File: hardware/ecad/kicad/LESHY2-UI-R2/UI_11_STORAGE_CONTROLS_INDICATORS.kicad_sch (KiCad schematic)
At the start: 107 parts, among them J4 Hirose DF40C(2.0)-40DS-0.4V(5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, J5 Hirose DM3AT-SF-PEJM5, Q1 Diodes Incorporated DMN2056U-7, SW10 OMRON B3S-1100P, SW11 OMRON B3S-1100P, SW12 OMRON B3S-1100P, SW13 OMRON B3S-1100P, SW14 OMRON B3S-1100P, SW15 OMRON B3S-1100P, SW16 OMRON B3S-1100P, SW17 OMRON B3S-1100P, SW3 OMRON B3S-1100P, SW4 OMRON B3S-1100P, SW5 OMRON B3S-1100P, SW6 OMRON B3S-1100P, SW7 OMRON B3S-1100P, SW8 OMRON B3S-1100P, SW9 OMRON B3S-1100P, U10 Texas Instruments TPS22919DCKR, U11 SN74LVC1G07DCKR, U12 Texas Instruments TPD8E003DQDR, U13 TCA9539PWR, U4 Texas Instruments TPS2553DRVR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, U5 Texas Instruments TPD8E003DQDR, U6 Texas Instruments TPD4E05U06D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, U7 Texas Instruments TPD4E05U06D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, U8 SN74LVC3G34DCUR, U9 Texas Instruments SN74LVC1G12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

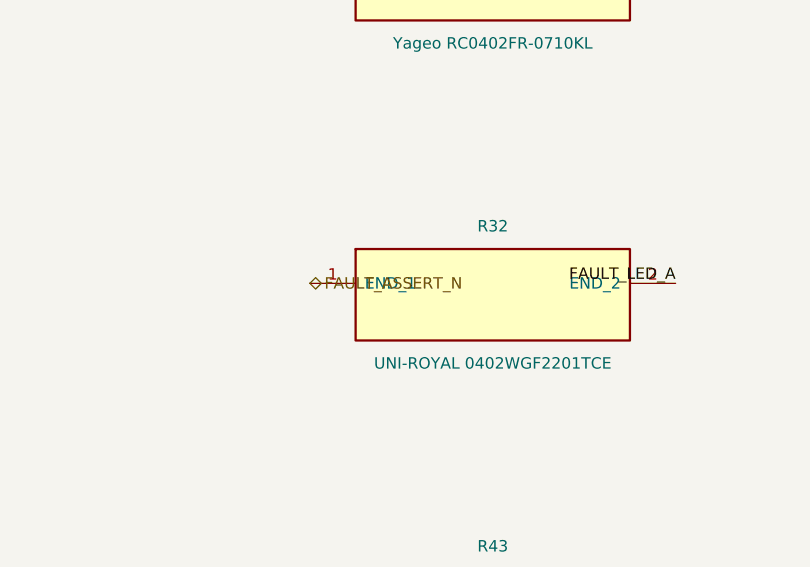
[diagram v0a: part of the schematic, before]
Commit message: Review R2 power transitions and watchdog
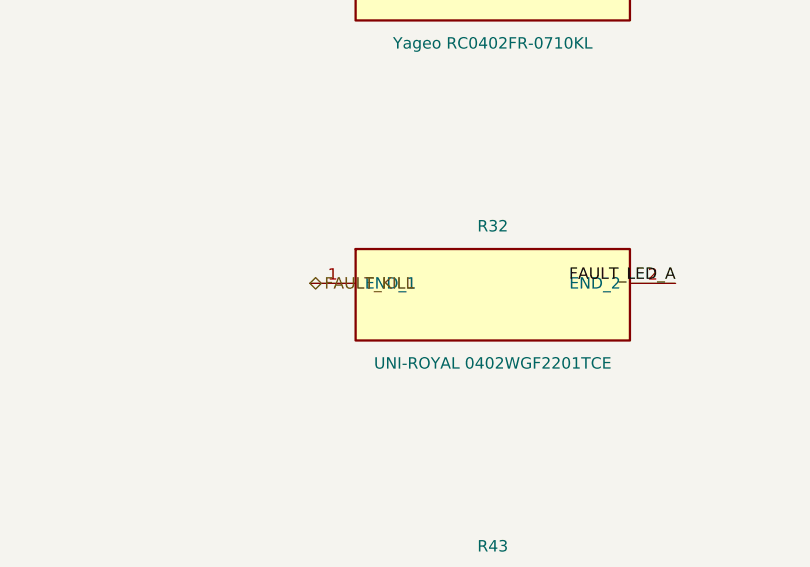
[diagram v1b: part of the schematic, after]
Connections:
- net FAULT_ASSERT_N renamed FAULT_KILL
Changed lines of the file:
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@@
 		)
 	)
-	(hierarchical_label "FAULT_ASSERT_N"
+	(hierarchical_label "FAULT_KILL"
 		(shape bidirectional)
 		(at 401.32 157.48 0)

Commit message: Review H3-R2.3 analog corners
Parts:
- R25: value Yageo RC0402JR-070RL -> FH RS-06L2R70FT; footprint Resistor_SMD:R_0402_1005Metric -> Resistor_SMD:R_1206_3216Metric; symbol Leshy2_R2:yageo_rc0402jr_070rl -> Leshy2_R2:fh_rs_06l2r70ft
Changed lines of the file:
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@@
 	)
 	(symbol
-		(lib_id "Leshy2_R2:yageo_rc0402jr_070rl")
+		(lib_id "Leshy2_R2:fh_rs_06l2r70ft")
 		(at 695.96 123.19 0)
 		(unit 1)
@@
 			(effects (font (size 1.27 1.27)))
 		)
-		(property "Value" "Yageo RC0402JR-070RL"
+		(property "Value" "FH RS-06L2R70FT"
 			(at 695.96 130.81 0)
 			(show_name no)
@@
 			(effects (font (size 1.27 1.27)))
 		)
-		(property "Footprint" "Resistor_SMD:R_0402_1005Metric"
+		(property "Footprint" "Resistor_SMD:R_1206_3216Metric"
 			(at 695.96 123.19 0)
 			(show_name no)
@@
 			(effects (font (size 1.27 1.27)))
 		)
-		(property "Description" "yageo_rc0402jr_070rl"
+		(property "Description" "fh_rs_06l2r70ft"
 			(at 695.96 123.19 0)
 			(show_name no)

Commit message: Mount display through direct UI-board ZIF
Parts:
- removed J4: Hirose DF40C(2.0)-40DS-0.4V(51), Connector_Hirose_DF40:Hirose_DF40C(2.0)-40DS-0.4V_2x20_P0.4mm, symbol Leshy2_R2:hirose_df40c_2_0_40ds_0_4v_51
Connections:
- no-connect marks 22 -> 11
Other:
- moved on the sheet: J5, Q1, R21, R22, R23, R24, R25, R26, R27, R28, R29, R30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

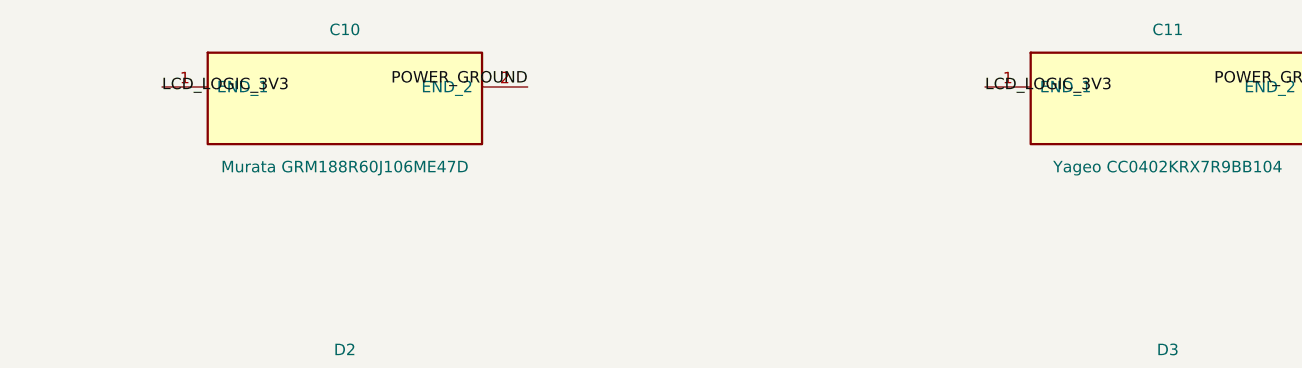
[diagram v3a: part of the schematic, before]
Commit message: Complete current R2 schematic and sourcing revalidation
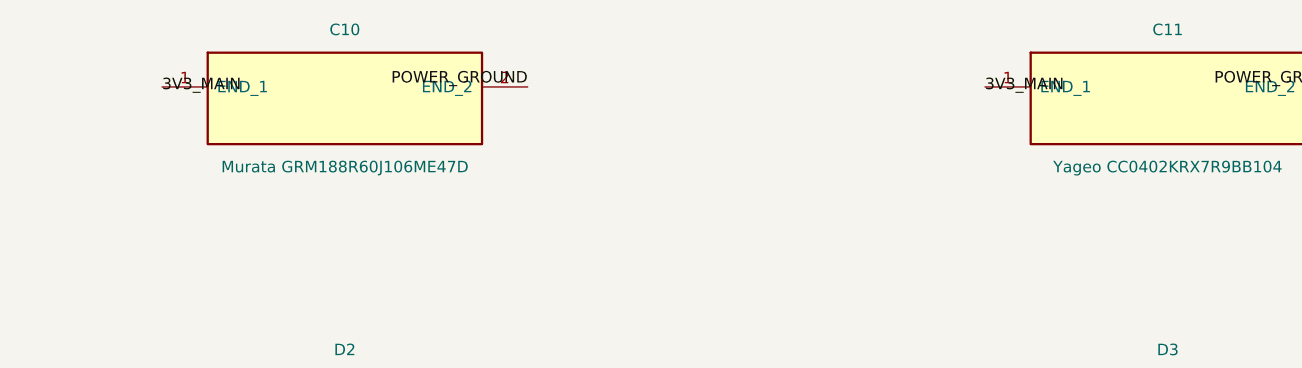
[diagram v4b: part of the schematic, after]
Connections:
- net LCD_LOGIC_3V3 is gone; now on net 3V3_MAIN: C10.1 (END_1), C11.1 (END_1)
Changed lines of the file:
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@@
 		)
 	)
-	(label "LCD_LOGIC_3V3"
+	(label "3V3_MAIN"
 		(at 309.88 50.80 0)
 		(effects (font (size 1.27 1.27)))
@@
 		)
 	)
-	(label "LCD_LOGIC_3V3"
+	(label "3V3_MAIN"
 		(at 401.32 50.80 0)
 		(effects (font (size 1.27 1.27)))

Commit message: Canonicalize physical ground anchors
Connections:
- net SAFETY_GROUND is gone; now on net POWER_GROUND: C20.2 (END_2), R73.2 (END_2)
- net SD_ESD_GROUND_A is gone; now on net POWER_GROUND: U6.3 (GND_3), U6.8 (GND_8)
- net SD_ESD_GROUND_B is gone; now on net POWER_GROUND: U7.3 (GND_3), U7.8 (GND_8)
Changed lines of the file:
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@@
 		(effects (font (size 1.27 1.27)))
 	)
-	(hierarchical_label "SAFETY_GROUND"
-		(shape bidirectional)
+	(label "POWER_GROUND"
 		(at 167.64 86.36 180)
 		(effects (font (size 1.27 1.27)) (justify right bottom))
@@
 		(effects (font (size 1.27 1.27)))
 	)
-	(label "SAFETY_GROUND"
+	(label "POWER_GROUND"
 		(at 716.28 264.16 180)
 		(effects (font (size 1.27 1.27)) (justify right bottom))
@@
 		(effects (font (size 1.27 1.27)))
 	)
-	(label "SD_ESD_GROUND_A"
+	(label "POWER_GROUND"
 		(at 309.88 337.82 0)
 		(effects (font (size 1.27 1.27)))
@@
 	(no_connect (at 350.52 335.28)
 	)
-	(label "SD_ESD_GROUND_A"
+	(label "POWER_GROUND"
 		(at 350.52 337.82 180)
 		(effects (font (size 1.27 1.27)) (justify right bottom))
@@
 		(effects (font (size 1.27 1.27)))
 	)
-	(label "SD_ESD_GROUND_B"
+	(label "POWER_GROUND"
 		(at 401.32 337.82 0)
 		(effects (font (size 1.27 1.27)))
@@
 	(no_connect (at 441.96 335.28)
 	)
-	(label "SD_ESD_GROUND_B"
+	(label "POWER_GROUND"
 		(at 441.96 337.82 180)
 		(effects (font (size 1.27 1.27)) (justify right bottom))

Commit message: Correct exact connector and protection geometry; expand electrical review
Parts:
- SW10, SW11, SW12, SW13, SW14, SW15, SW16, SW17, SW3, SW4, SW5, SW6, SW7, SW8, SW9: footprint Leshy2:B3S-1100P -> Leshy2_R2:B3S-1100P
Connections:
- net POWER_GROUND: now also J5.9 (DETECT_B), SW10.1 (SIDE_B_2), SW11.1 (SIDE_B_2), SW12.1 (SIDE_B_2), SW13.1 (SIDE_B_2), SW14.1 (SIDE_B_2), SW15.1 (SIDE_B_2), SW16.1 (SIDE_B_2), SW17.1 (SIDE_B_2), SW3.1 (SIDE_B_2), SW4.1 (SIDE_B_2), SW5.1 (SIDE_B_2), SW6.1 (SIDE_B_2), SW7.1 (SIDE_B_2), SW8.1 (SIDE_B_2), SW9.1 (SIDE_B_2); no longer J5.10 (DETECT_B), SW10.4 (SIDE_B_2), SW11.4 (SIDE_B_2), SW12.4 (SIDE_B_2), SW13.4 (SIDE_B_2), SW14.4 (SIDE_B_2), SW15.4 (SIDE_B_2), SW16.4 (SIDE_B_2), SW17.4 (SIDE_B_2), SW3.4 (SIDE_B_2), SW4.4 (SIDE_B_2), SW5.4 (SIDE_B_2), SW6.4 (SIDE_B_2), SW7.4 (SIDE_B_2), SW8.4 (SIDE_B_2), SW9.4 (SIDE_B_2)
- net SD_CARD_DETECT_RAW_N: now also J5.10 (DETECT_A); no longer J5.9 (DETECT_A)
- net UI_BACK_N: now also SW8.4 (SIDE_A_1); no longer SW8.1 (SIDE_A_1)
- net UI_DPAD_DOWN_N: now also SW3.4 (SIDE_A_1); no longer SW3.1 (SIDE_A_1)
- net UI_DPAD_LEFT_N: now also SW4.4 (SIDE_A_1); no longer SW4.1 (SIDE_A_1)
- net UI_DPAD_OK_N: now also SW5.4 (SIDE_A_1); no longer SW5.1 (SIDE_A_1)
- net UI_DPAD_RIGHT_N: now also SW6.4 (SIDE_A_1); no longer SW6.1 (SIDE_A_1)
- net UI_DPAD_UP_N: now also SW7.4 (SIDE_A_1); no longer SW7.1 (SIDE_A_1)
- net UI_F1_N: now also SW9.4 (SIDE_A_1); no longer SW9.1 (SIDE_A_1)
- net UI_F2_N: now also SW10.4 (SIDE_A_1); no longer SW10.1 (SIDE_A_1)
- net UI_F3_N: now also SW11.4 (SIDE_A_1); no longer SW11.1 (SIDE_A_1)
- net UI_F4_N: now also SW12.4 (SIDE_A_1); no longer SW12.1 (SIDE_A_1)
- net UI_F5_N: now also SW13.4 (SIDE_A_1); no longer SW13.1 (SIDE_A_1)
- net UI_F6_N: now also SW14.4 (SIDE_A_1); no longer SW14.1 (SIDE_A_1)
- net UI_F7_N: now also SW15.4 (SIDE_A_1); no longer SW15.1 (SIDE_A_1)
- net UI_F8_N: now also SW16.4 (SIDE_A_1); no longer SW16.1 (SIDE_A_1)
- net UI_OPT_N: now also SW17.4 (SIDE_A_1); no longer SW17.1 (SIDE_A_1)
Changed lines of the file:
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@@
 		(effects (font (size 1.27 1.27)) (justify right bottom))
 	)
-	(label "SD_CARD_DETECT_RAW_N"
+	(label "POWER_GROUND"
 		(at 76.20 124.46 180)
 		(effects (font (size 1.27 1.27)) (justify right bottom))
 	)
-	(label "POWER_GROUND"
+	(label "SD_CARD_DETECT_RAW_N"
 		(at 76.20 127.00 180)
 		(effects (font (size 1.27 1.27)) (justify right bottom))
@@
 			(effects (font (size 1.27 1.27)))
 		)
-		(property "Footprint" "Leshy2:B3S-1100P"
+		(property "Footprint" "Leshy2_R2:B3S-1100P"
 			(at 970.28 265.43 0)
 			(show_name no)
@@
 		)
 	)
-	(label "UI_DPAD_DOWN_N"
+	(label "POWER_GROUND"
 		(at 949.96 262.89 0)
 		(effects (font (size 1.27 1.27)))
@@
 		(effects (font (size 1.27 1.27)))
 	)
-	(label "POWER_GROUND"
+	(label "UI_DPAD_DOWN_N"
 		(at 990.60 262.89 180)
 		(effects (font (size 1.27 1.27)) (justify right bottom))
@@
 			(effects (font (size 1.27 1.27)))
 		)
-		(property "Footprint" "Leshy2:B3S-1100P"
+		(property "Footprint" "Leshy2_R2:B3S-1100P"
 			(at 1061.72 265.43 0)
 			(show_name no)
@@
 		)
 	)
-	(label "UI_DPAD_LEFT_N"
+	(label "POWER_GROUND"
 		(at 1041.40 262.89 0)
 		(effects (font (size 1.27 1.27)))
@@
 		(effects (font (size 1.27 1.27)))
 	)
-	(label "POWER_GROUND"
+	(label "UI_DPAD_LEFT_N"
 		(at 1082.04 262.89 180)
 		(effects (font (size 1.27 1.27)) (justify right bottom))
@@
 			(effects (font (size 1.27 1.27)))
 		)
-		(property "Footprint" "Leshy2:B3S-1100P"
+		(property "Footprint" "Leshy2_R2:B3S-1100P"
 			(at 55.88 270.51 0)
 			(show_name no)
@@
 		)
 	)
-	(label "UI_DPAD_OK_N"
+	(label "POWER_GROUND"
 		(at 35.56 267.97 0)
 		(effects (font (size 1.27 1.27)))
@@
 		(effects (font (size 1.27 1.27)))
 	)
-	(label "POWER_GROUND"
+	(label "UI_DPAD_OK_N"
 		(at 76.20 267.97 180)
 		(effects (font (size 1.27 1.27)) (justify right bottom))
@@
 			(effects (font (size 1.27 1.27)))
 		)
-		(property "Footprint" "Leshy2:B3S-1100P"
+		(property "Footprint" "Leshy2_R2:B3S-1100P"
 			(at 147.32 300.99 0)
 			(show_name no)
@@
 		)
 	)
-	(label "UI_DPAD_RIGHT_N"
+	(label "POWER_GROUND"
 		(at 127.00 298.45 0)
 		(effects (font (size 1.27 1.27)))
@@
 		(effects (font (size 1.27 1.27)))
 	)
-	(label "POWER_GROUND"
+	(label "UI_DPAD_RIGHT_N"
 		(at 167.64 298.45 180)
 		(effects (font (size 1.27 1.27)) (justify right bottom))
@@
 			(effects (font (size 1.27 1.27)))
 		)
-		(property "Footprint" "Leshy2:B3S-1100P"
+		(property "Footprint" "Leshy2_R2:B3S-1100P"
 			(at 238.76 300.99 0)
 			(show_name no)
@@
 		)
 	)
-	(label "UI_DPAD_UP_N"
+	(label "POWER_GROUND"
 		(at 218.44 298.45 0)
 		(effects (font (size 1.27 1.27)))
@@
 		(effects (font (size 1.27 1.27)))
 	)
-	(label "POWER_GROUND"
+	(label "UI_DPAD_UP_N"
 		(at 259.08 298.45 180)
 		(effects (font (size 1.27 1.27)) (justify right bottom))
@@
 			(effects (font (size 1.27 1.27)))
 		)
-		(property "Footprint" "Leshy2:B3S-1100P"
+		(property "Footprint" "Leshy2_R2:B3S-1100P"
 			(at 330.20 300.99 0)
 			(show_name no)
@@
 		)
 	)
-	(label "UI_BACK_N"
+	(label "POWER_GROUND"
 		(at 309.88 298.45 0)
 		(effects (font (size 1.27 1.27)))
@@
 		(effects (font (size 1.27 1.27)))
 	)
-	(label "POWER_GROUND"
+	(label "UI_BACK_N"
 		(at 350.52 298.45 180)
 		(effects (font (size 1.27 1.27)) (justify right bottom))
@@
 			(effects (font (size 1.27 1.27)))
 		)
-		(property "Footprint" "Leshy2:B3S-1100P"
+		(property "Footprint" "Leshy2_R2:B3S-1100P"
 			(at 421.64 300.99 0)
 			(show_name no)
@@
 		)
 	)
-	(label "UI_F1_N"
+	(label "POWER_GROUND"
 		(at 401.32 298.45 0)
 		(effects (font (size 1.27 1.27)))
@@
 		(effects (font (size 1.27 1.27)))
 	)
-	(label "POWER_GROUND"
+	(label "UI_F1_N"
 		(at 441.96 298.45 180)
 		(effects (font (size 1.27 1.27)) (justify right bottom))
@@
 			(effects (font (size 1.27 1.27)))
 		)
-		(property "Footprint" "Leshy2:B3S-1100P"
+		(property "Footprint" "Leshy2_R2:B3S-1100P"
 			(at 513.08 300.99 0)
 			(show_name no)
@@
 		)
 	)
-	(label "UI_F2_N"
+	(label "POWER_GROUND"
 		(at 492.76 298.45 0)
 		(effects (font (size 1.27 1.27)))
@@
 		(effects (font (size 1.27 1.27)))
 	)
-	(label "POWER_GROUND"
+	(label "UI_F2_N"
 		(at 533.40 298.45 180)
 		(effects (font (size 1.27 1.27)) (justify right bottom))
@@
 			(effects (font (size 1.27 1.27)))
 		)
-		(property "Footprint" "Leshy2:B3S-1100P"
+		(property "Footprint" "Leshy2_R2:B3S-1100P"
 			(at 604.52 300.99 0)
 			(show_name no)
@@
 		)
 	)
-	(label "UI_F3_N"
+	(label "POWER_GROUND"
 		(at 584.20 298.45 0)
 		(effects (font (size 1.27 1.27)))
@@
 		(effects (font (size 1.27 1.27)))
 	)
-	(label "POWER_GROUND"
+	(label "UI_F3_N"
 		(at 624.84 298.45 180)
 		(effects (font (size 1.27 1.27)) (justify right bottom))
@@
 			(effects (font (size 1.27 1.27)))
 		)
-		(property "Footprint" "Leshy2:B3S-1100P"
+		(property "Footprint" "Leshy2_R2:B3S-1100P"
 			(at 695.96 300.99 0)
 			(show_name no)
@@
 		)
 	)
-	(label "UI_F4_N"
+	(label "POWER_GROUND"
 		(at 675.64 298.45 0)
 		(effects (font (size 1.27 1.27)))
@@
 		(effects (font (size 1.27 1.27)))
 	)
-	(label "POWER_GROUND"
+	(label "UI_F4_N"
 		(at 716.28 298.45 180)
 		(effects (font (size 1.27 1.27)) (justify right bottom))
@@
 			(effects (font (size 1.27 1.27)))
 		)
-		(property "Footprint" "Leshy2:B3S-1100P"
+		(property "Footprint" "Leshy2_R2:B3S-1100P"
 			(at 787.40 300.99 0)
 			(show_name no)
@@
 		)
 	)
-	(label "UI_F5_N"
+	(label "POWER_GROUND"
 		(at 767.08 298.45 0)
 		(effects (font (size 1.27 1.27)))
@@
 		(effects (font (size 1.27 1.27)))
 	)
-	(label "POWER_GROUND"
+	(label "UI_F5_N"
 		(at 807.72 298.45 180)
 		(effects (font (size 1.27 1.27)) (justify right bottom))
@@
 			(effects (font (size 1.27 1.27)))
 		)
-		(property "Footprint" "Leshy2:B3S-1100P"
+		(property "Footprint" "Leshy2_R2:B3S-1100P"
 			(at 878.84 300.99 0)
 			(show_name no)
@@
 		)
 	)
-	(label "UI_F6_N"
+	(label "POWER_GROUND"
 		(at 858.52 298.45 0)
 		(effects (font (size 1.27 1.27)))
@@
 		(effects (font (size 1.27 1.27)))
 	)
-	(label "POWER_GROUND"
+	(label "UI_F6_N"
 		(at 899.16 298.45 180)
 		(effects (font (size 1.27 1.27)) (justify right bottom))
@@
 			(effects (font (size 1.27 1.27)))
 		)
-		(property "Footprint" "Leshy2:B3S-1100P"
+		(property "Footprint" "Leshy2_R2:B3S-1100P"
 			(at 970.28 300.99 0)
 			(show_name no)
@@
 		)
 	)
-	(label "UI_F7_N"
+	(label "POWER_GROUND"
 		(at 949.96 298.45 0)
 		(effects (font (size 1.27 1.27)))
@@
 		(effects (font (size 1.27 1.27)))
 	)
-	(label "POWER_GROUND"
+	(label "UI_F7_N"
 		(at 990.60 298.45 180)
 		(effects (font (size 1.27 1.27)) (justify right bottom))
@@
 			(effects (font (size 1.27 1.27)))
 		)
-		(property "Footprint" "Leshy2:B3S-1100P"
+		(property "Footprint" "Leshy2_R2:B3S-1100P"
 			(at 1061.72 300.99 0)
 			(show_name no)
@@
 		)
 	)
-	(label "UI_F8_N"
+	(label "POWER_GROUND"
 		(at 1041.40 298.45 0)
 		(effects (font (size 1.27 1.27)))
@@
 		(effects (font (size 1.27 1.27)))
 	)
-	(label "POWER_GROUND"
+	(label "UI_F8_N"
 		(at 1082.04 298.45 180)
 		(effects (font (size 1.27 1.27)) (justify right bottom))
@@
 			(effects (font (size 1.27 1.27)))
 		)
-		(property "Footprint" "Leshy2:B3S-1100P"
+		(property "Footprint" "Leshy2_R2:B3S-1100P"
 			(at 55.88 306.07 0)
 			(show_name no)
@@
 		)
 	)
-	(label "UI_OPT_N"
+	(label "POWER_GROUND"
 		(at 35.56 303.53 0)
 		(effects (font (size 1.27 1.27)))
@@
 		(effects (font (size 1.27 1.27)))
 	)
-	(label "POWER_GROUND"
+	(label "UI_OPT_N"
 		(at 76.20 303.53 180)
 		(effects (font (size 1.27 1.27)) (justify right bottom))
